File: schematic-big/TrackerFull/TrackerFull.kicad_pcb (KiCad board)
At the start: 2 copper layers, 43.2 x 38.1 mm, 58 parts, among them J1 Conn_01x05_Male, J3 Screw_Terminal_01x02, J4 78646-3001, J5 Screw_Terminal_01x02, Q1 IRLML0030, Q2 IRLML5203, Q3 IRLML5203, SW1 SW_Push, U1 LP2985-3.3, U2 LIS3DSH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

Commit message: last changes
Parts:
- moved GSM1 1.33 mm to (203.9, 96.0)
- moved H4 0.28 mm to (202.3, 71.5)
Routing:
- net GNDREF: track 195.4 -> 256.1 mm, vias 28 -> 32
- net /ACCEL_INT1: track 41.3 -> 98.0 mm, vias 2 -> 3
- net /VBAT: track 19.1 -> 60.5 mm, vias 0 -> 3
- net /SIM_RST: track 0.00 -> 24.3 mm
- net /VSIM: track 0.00 -> 17.6 mm
- net /AVR_RST: track 10.4 -> 25.1 mm, vias 0 -> 2
- net /ACCEL_INT2: track 25.9 -> 34.4 mm
- net /SIM_IO: track 15.5 -> 21.1 mm
- net /V_BAT: track 23.9 -> 19.3 mm
- net BAT_IN: track 77.6 -> 81.0 mm, vias 4 -> 5
- net Net-(D1-Pad45): track 3.20 -> 1.76 mm
- net +5V: track 47.0 -> 48.2 mm
- net /ACCEL_SCL: track 8.27 -> 7.08 mm
- net /AVR_MOSI_SDA: track 26.4 -> 27.1 mm
- net /SIM_CLK: track 16.0 -> 16.6 mm
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- added copper zone on B.Cu, net BAT_IN
- added copper zone on F.Cu, net GNDREF
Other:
- outline, holes or cut-outs redrawn
- net class Default: clearance 0.2 -> 0.127
- rule trace_clearance: 0.2 -> 0.127
- rule trace_min: 0.2 -> 0.127
- rule via_min_drill: 0.3 -> 0.2
- rule via_min_size: 0.4 -> 0.2

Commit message: last changes
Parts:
- C1: value 4.7u -> 4.7uF
- C10: footprint Capacitor_SMD:C_0201_0603Metric -> Capacitor_SMD:C_0402_1005Metric
- C11, C18: footprint Capacitor_Tantalum_SMD:CP_EIA-3216-18_Kemet-A -> Capacitor_SMD:C_0603_1608Metric
- C12: footprint Capacitor_SMD:C_1206_3216Metric_Pad1.42x1.75mm_HandSolder -> Capacitor_Tantalum_SMD:CP_EIA-7343-31_Kemet-D
- C17: footprint Capacitor_SMD:C_1206_3216Metric_Pad1.42x1.75mm_HandSolder -> Capacitor_SMD:C_0603_1608Metric; moved to B.Cu
- C6: value C -> 4.7uF
- R10: value 100kOm -> 100K; footprint Resistor_SMD:R_0603_1608Metric -> Resistor_SMD:R_0805_2012Metric_Pad1.15x1.40mm_HandSolder
- R13, R17, R4: footprint Resistor_SMD:R_0603_1608Metric -> Resistor_SMD:R_0805_2012Metric_Pad1.15x1.40mm_HandSolder
- R14, R16: value 10000 -> 10K; footprint Resistor_SMD:R_0603_1608Metric -> Resistor_SMD:R_0805_2012Metric_Pad1.15x1.40mm_HandSolder
- R15: value 43000 -> 43K
- moved C17 13.1 mm to (199.6, 68.0), turned to 180 degrees
- moved C10 5.09 mm to (182.5, 79.6)
- moved C12 1.84 mm to (186.0, 75.7)
- moved Q2 0.73 mm to (178.4, 80.8)
- moved R2 0.40 mm to (181.7, 81.0), turned to 0 degrees
- moved D2 0.26 mm to (185.4, 75.7)
- moved R13 0.25 mm to (174.6, 102.1)
- moved R17 0.20 mm to (192.8, 80.1)
- moved C14 0.14 mm to (184.8, 81.0)
- moved C8 0.06 mm to (187.4, 81.0)
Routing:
- net GNDREF: track 256.1 -> 241.7 mm
- net Net-(C17-Pad2): track 2.04 -> 14.9 mm, vias 0 -> 1
- net Net-(D1-Pad15): track 4.34 -> 5.27 mm
- net /ACCEL_INT1: track 98.0 -> 98.9 mm
- net /VBAT: track 60.5 -> 59.7 mm
- net Net-(Q1-Pad3): track 13.7 -> 13.0 mm
- net BAT_IN: track 81.0 -> 81.6 mm

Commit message: schematic updated
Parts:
- added C19: 1uF, Capacitor_SMD:C_0603_1608Metric, F.Cu at (168.0, 93.0)
- added R5: 10K, Resistor_SMD:R_0805_2012Metric_Pad1.15x1.40mm_HandSolder, B.Cu at (175.4, 93.2)
- added R6: 470, Resistor_SMD:R_0603_1608Metric, F.Cu at (177.1, 99.2)
- added U7: MIC5504-3.3YM5, Package_TO_SOT_SMD:SOT-23-5, F.Cu at (163.8, 94.8)
- C1: value 4.7uF -> 2.2uF
- C12: footprint Capacitor_Tantalum_SMD:CP_EIA-7343-31_Kemet-D -> Capacitor_Tantalum_SMD:CP_EIA-6032-28_Kemet-C
- C17, D3: moved to F.Cu
- C2: footprint Capacitor_SMD:C_0603_1608Metric -> Capacitor_SMD:C_0805_2012Metric
- Q1: value IRLML0030 -> DMG2305UXQ
- Q2, Q3: value IRLML5203 -> DMG2305UXQ
- R10: value 100K -> 10K
- R12, R8: value 250 -> 150
- R3: value 10K -> 470; footprint Resistor_SMD:R_0805_2012Metric_Pad1.15x1.40mm_HandSolder -> Resistor_SMD:R_0603_1608Metric
- SW1: value SW_Push -> PTS647SK38SMTR2LFS; footprint Button_Switch_SMD:SW_Push_1P1T_NO_6x6mm_H9.5mm -> imported:PTS647SK38SMTR2LFS
- U1: value LP2985-3.3 -> LP2980IM5-3.6
- moved Q1 17.9 mm to (174.5, 100.5)
- moved C17 13.1 mm to (187.1, 71.6), turned to 0 degrees
- moved C4 7.22 mm to (177.0, 89.6), turned to 270 degrees
- moved Q3 5.89 mm to (171.8, 78.5)
- moved R3 5.51 mm to (170.5, 83.8)
- moved SW1 0.81 mm to (181.6, 94.8)
- moved C12 0.65 mm to (186.3, 76.3)
- moved C18 0.52 mm to (193.7, 75.9)
- moved D3 0.42 mm to (166.3, 76.4)
- renumbered GSM1 to U6
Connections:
- net /3.3v renamed /3.6v
- C9 pad 1: /VBAT -> Net-(C9-Pad1)
- D1 pad 23: (no net) -> /GPS_POWER
- D1 pad 51: /ACCEL_INT1 -> (no net)
- Q1 pad 1: /PWR_CTRL -> Net-(Q1-Pad1)
- Q1 pad 2: GNDREF -> /VBAT
- Q1 pad 3: Net-(Q1-Pad3) -> Net-(C9-Pad1)
- Q2 pad 1: Net-(Q1-Pad3) -> /PWR_CTRL
- R13 pad 1: /VBAT -> Net-(C9-Pad1)
- R3 pad 1: BAT_IN -> /PWR_CTRL
- R3 pad 2: Net-(Q1-Pad3) -> Net-(R3-Pad2)
- SW1 pad 2: GNDREF -> /AVR_RST
- U3 pad 3: /PWR_CTRL -> Net-(R3-Pad2)
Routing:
- net /ACCEL_INT1: track 98.9 -> 13.2 mm, vias 3 -> 0
- net Net-(C17-Pad2): track 14.9 -> 1.71 mm, vias 1 -> 0
- net Net-(Q1-Pad3): track 13.0 -> 0.00 mm, vias 2 -> 0
- net GNDREF: track 241.7 -> 253.7 mm, vias 32 -> 34
- net +5V: track 48.2 -> 58.6 mm, vias 4 -> 3
- net /GPS_POWER: track 0.00 -> 7.03 mm
- net /V_BAT: track 19.3 -> 13.6 mm
- net BAT_IN: track 81.6 -> 76.6 mm
- net /ACCEL_CS: track 6.77 -> 10.7 mm, vias 0 -> 1
- net /ACCEL_INT2: track 34.4 -> 30.5 mm
- net /AVR_RST: track 25.1 -> 21.8 mm, vias 2 -> 0
- net Net-(R3-Pad2): track 0.00 -> 2.60 mm
- net /CHARGER_VDD: track 33.3 -> 35.7 mm, vias 8 -> 6
- net /PWR_CTRL: track 8.43 -> 10.8 mm
- net Net-(C9-Pad1): track 0.00 -> 2.19 mm, vias 0 -> 1
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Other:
- board size 43.2 x 38.1 mm -> 43.2 x 38 mm
- rule via_min_drill: 0.2 -> 0.3
- rule via_min_size: 0.2 -> 0.3

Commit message: next milestone
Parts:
- removed C13, C9: 4.7uF, Capacitor_SMD:C_0603_1608Metric
- removed Q1: DMG2305UXQ, Package_TO_SOT_SMD:SOT-23
- removed R13: 100K, Resistor_SMD:R_0805_2012Metric_Pad1.15x1.40mm_HandSolder
- removed R6: 470, Resistor_SMD:R_0603_1608Metric
- added ANT1: 1462350001, imported:ANT_1462350001, B.Cu at (167.3, 101.3)
- added L3: LQG15HS1N8B02, Inductor_SMD:L_0402_1005Metric, B.Cu at (178.7, 99.1)
- added U8: AP62301, Package_TO_SOT_SMD:SOT-563, F.Cu at (222.7, 79.2)
- C1: value 2.2uF -> 0.47uF
- H3, H4: moved to B.Cu
- L1: value LQG15HN27NJ -> LQG15HS5N1B02; footprint Inductor_SMD:L_01005_0402Metric -> Inductor_SMD:L_0402_1005Metric
- L2: value IHLP1212BZER2R2M11 -> MDWK4040T3R3MM; footprint Inductor_SMD:L_Vishay_IHLP-1212 -> Inductor_SMD:L_Taiyo-Yuden_MD-4040
- U1: value LP2980IM5-3.6 -> TLV62568DBV
- U5: value U.FL -> BGU7007,115; footprint mailboxNotifier:U.FL -> imported:PSON50P100X145X50-6N
- U7: value MIC5504-3.3YM5 -> MIC5232-2.5YD5
- moved U1 45.3 mm to (214.4, 82.8), turned to 0 degrees
- moved L1 8.83 mm to (170.6, 101.5)
- moved H3 7.08 mm to (175.6, 101.6)
- moved U7 6.58 mm to (170.4, 94.7), turned to 270 degrees
- moved U5 6.52 mm to (171.8, 99.8)
- moved D3 5.71 mm to (171.6, 78.6), turned to 180 degrees
- moved R11 5.35 mm to (170.5, 86.8), turned to 0 degrees
- moved Q3 5.30 mm to (177.1, 78.6)
- moved C19 2.53 mm to (170.3, 91.9), turned to 0 degrees
- moved Q2 1.90 mm to (178.4, 82.7)
- moved H4 1.62 mm to (202.6, 69.9)
- moved J1 1.21 mm to (203.6, 80.7)
- moved R1 1.16 mm to (172.2, 84.9)
- moved R3 0.73 mm to (170.6, 83.1)
- moved R15 0.56 mm to (197.4, 68.9)
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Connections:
- C1 pad 1: /3.6v -> /2.5v
- C2 pad 2: /3.6v -> /2.5v
- C3 pad 2: /3.6v -> /2.5v
- L1 pad 2: /GPS_RF -> Net-(L1-Pad2)
- U1 pad 1: BAT_IN -> (no net)
- U1 pad 2: GNDREF -> (no net)
- U1 pad 3: BAT_IN -> (no net)
- U1 pad 5: /3.6v -> (no net)
- U2 pad 1: /3.6v -> /2.5v
- U2 pad 14: /3.6v -> /2.5v
- U2 pad 15: /3.6v -> /2.5v
- U5 pad 3: /GPS_RF -> Net-(L1-Pad2)
- U7 pad 1: (no net) -> BAT_IN
- U7 pad 2: (no net) -> GNDREF
- U7 pad 3: (no net) -> BAT_IN
- U7 pad 5: (no net) -> /2.5v
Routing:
- net GNDREF: track 253.7 -> 207.8 mm, vias 34 -> 29
- net /VBAT: track 58.2 -> 38.7 mm
- net /2.5v: track 0.00 -> 13.1 mm
- net /3.6v: track 13.1 -> 0.00 mm
- net +5V: track 58.6 -> 47.1 mm, vias 3 -> 2
- net /LED_CTL: track 14.5 -> 7.71 mm
- net BAT_IN: track 76.6 -> 71.9 mm, vias 5 -> 4
- net /GPS_RF: track 6.27 -> 2.14 mm
- net Net-(ANT1-Pad1): track 7.57 -> 3.89 mm, vias 2 -> 0
- net /PWR_CTRL: track 10.8 -> 8.30 mm
- net /CHARGER_VDD: track 35.7 -> 38.0 mm
- net Net-(C9-Pad1): track 2.19 -> 0.00 mm, vias 1 -> 0
- net Net-(Q1-Pad1): track 1.83 -> 0.00 mm
- net /V_BAT: track 13.6 -> 11.8 mm
- net Net-(L1-Pad2): track 0.00 -> 1.43 mm
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- added copper zone on F.Cu, net BAT_IN
- removed copper zone on B.Cu, net BAT_IN
- removed copper zone on F.Cu, net GNDREF
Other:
- board size 43.2 x 38 mm -> 41.1 x 38 mm

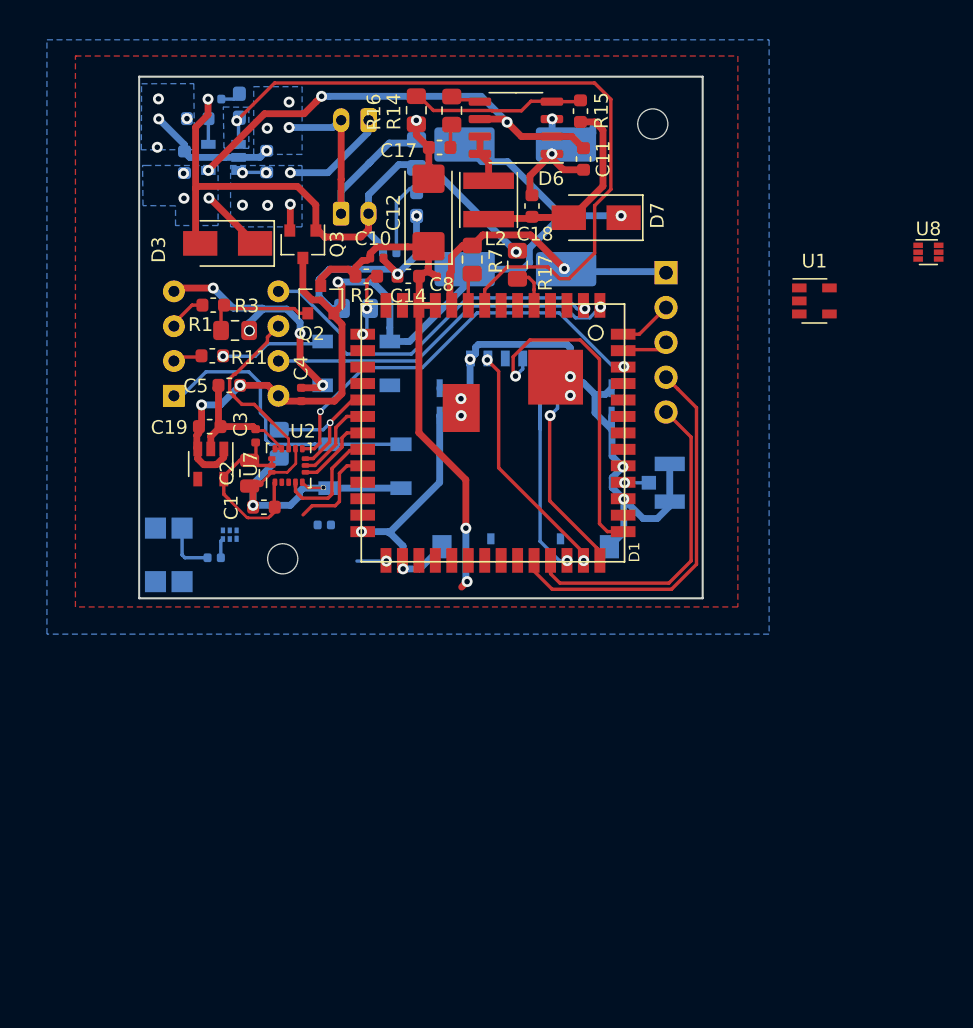
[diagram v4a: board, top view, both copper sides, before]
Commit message: GPS antenna on pcb
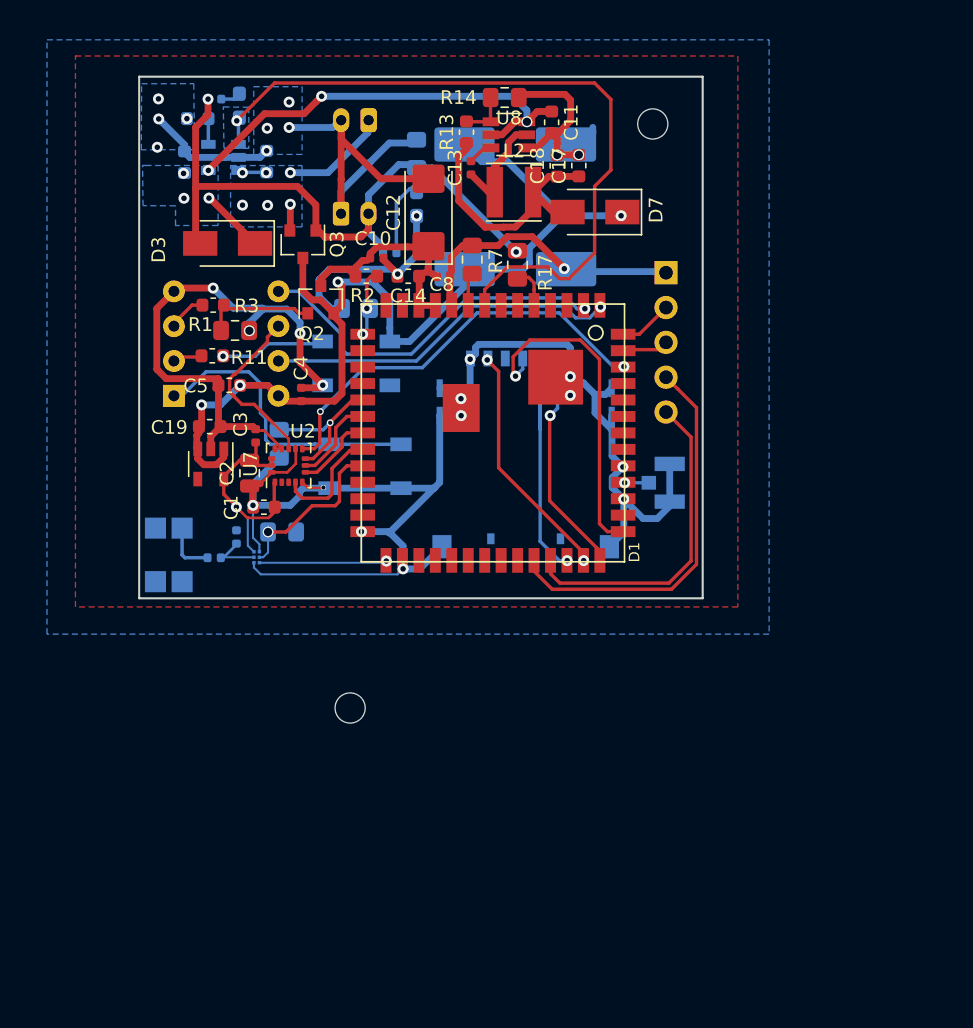
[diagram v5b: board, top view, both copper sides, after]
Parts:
- removed D6: APW7142, Package_SO:SOP-8_3.9x4.9mm_P1.27mm
- removed R15: 43K, Resistor_SMD:R_0603_1608Metric
- removed R16: 10K, Resistor_SMD:R_0805_2012Metric_Pad1.15x1.40mm_HandSolder
- removed U1: TLV62568DBV, Package_TO_SOT_SMD:SOT-23-5
- added C13: 100nF, Capacitor_SMD:C_0402_1005Metric, F.Cu at (189.4, 73.1)
- added R13: 43K, Resistor_SMD:R_0603_1608Metric, F.Cu at (189.0, 70.5)
- added R6: 10K, Resistor_SMD:R_0805_2012Metric_Pad1.15x1.40mm_HandSolder, B.Cu at (175.6, 99.6)
- C17: value 10uF -> 22uF
- J3: value Screw_Terminal_01x02 -> Battery
- J5: value Screw_Terminal_01x02 -> USB power
- U5: value BGU7007,115 -> BGU8019; footprint imported:PSON50P100X145X50-6N -> imported:SOT1232
- U8: footprint Package_TO_SOT_SMD:SOT-563 -> Package_TO_SOT_SMD:TSOT-23-6
- moved U8 31.8 mm to (192.1, 70.7), turned to 180 degrees
- moved H3 11.9 mm to (180.6, 112.5)
- moved C17 10.2 mm to (197.2, 72.9), turned to 90 degrees
- moved L3 6.46 mm to (172.3, 100.0), turned to 90 degrees
- moved R14 3.98 mm to (191.8, 67.9), turned to 0 degrees
- moved C11 3.54 mm to (195.2, 69.7)
- moved C18 3.46 mm to (195.6, 72.9)
- moved U5 2.56 mm to (173.7, 101.5), turned to 180 degrees
- moved L2 1.93 mm to (192.5, 74.8), turned to 0 degrees
- moved D7 0.42 mm to (198.4, 76.3)
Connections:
- C17 pad 1: GNDREF -> /APW_OUT
- C17 pad 2: Net-(C17-Pad2) -> GNDREF
- L1 pad 2: Net-(L1-Pad2) -> /GPS_SIGNAL
- L2 pad 1: /LX -> Net-(C13-Pad1)
- L3 pad 1: Net-(L1-Pad2) -> /GPS_SIGNAL
- R14 pad 1: Net-(D6-Pad5) -> Net-(R13-Pad2)
- R14 pad 2: Net-(C17-Pad2) -> GNDREF
- U5 pad 2: GNDREF -> /GPS_POWER
- U5 pad 3: Net-(L1-Pad2) -> /GPS_RF
- U5 pad 4: /VBAT -> GNDREF
- U5 pad 5: /GPS_POWER -> /GPS_SIGNAL
- U5 pad 6: /GPS_RF -> /2.5v
- U8 pad 1: (no net) -> GNDREF
- U8 pad 2: (no net) -> Net-(C13-Pad1)
- U8 pad 3: (no net) -> /CHARGER_VDD
- U8 pad 4: (no net) -> Net-(R13-Pad2)
- U8 pad 5: (no net) -> /CHARGER_VDD
- U8 pad 6: (no net) -> Net-(C13-Pad2)
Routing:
- net GNDREF: track 207.8 -> 244.6 mm, vias 29 -> 28
- net /VBAT: track 38.7 -> 16.6 mm, vias 2 -> 0
- net Net-(D6-Pad4): track 13.3 -> 0.00 mm
- net Net-(C13-Pad1): track 0.00 -> 7.88 mm
- net /GPS_RF: track 2.14 -> 9.31 mm
- net /GPS_POWER: track 7.03 -> 12.4 mm, vias 0 -> 1
- net /APW_OUT: track 15.4 -> 19.9 mm
- net /GPS_SIGNAL: track 0.00 -> 3.96 mm
- net /2.5v: track 13.1 -> 16.9 mm, vias 0 -> 1
- net Net-(R13-Pad2): track 0.00 -> 3.73 mm
- net /LX: track 3.54 -> 0.00 mm
- net Net-(D6-Pad5): track 2.11 -> 0.00 mm
- net Net-(C13-Pad2): track 0.00 -> 1.86 mm
- net Net-(C17-Pad2): track 1.71 -> 0.00 mm
- net Net-(L1-Pad2): track 1.43 -> 0.00 mm
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
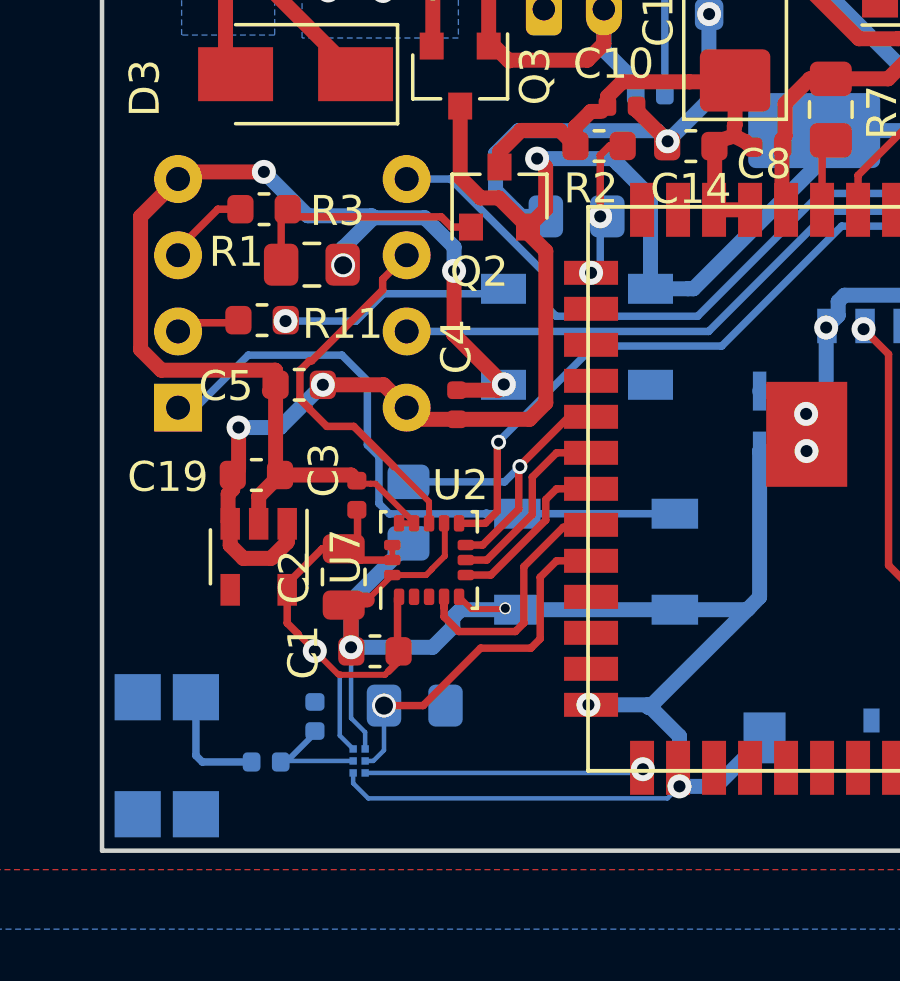
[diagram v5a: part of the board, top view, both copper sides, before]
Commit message: GPS antenna on pcb
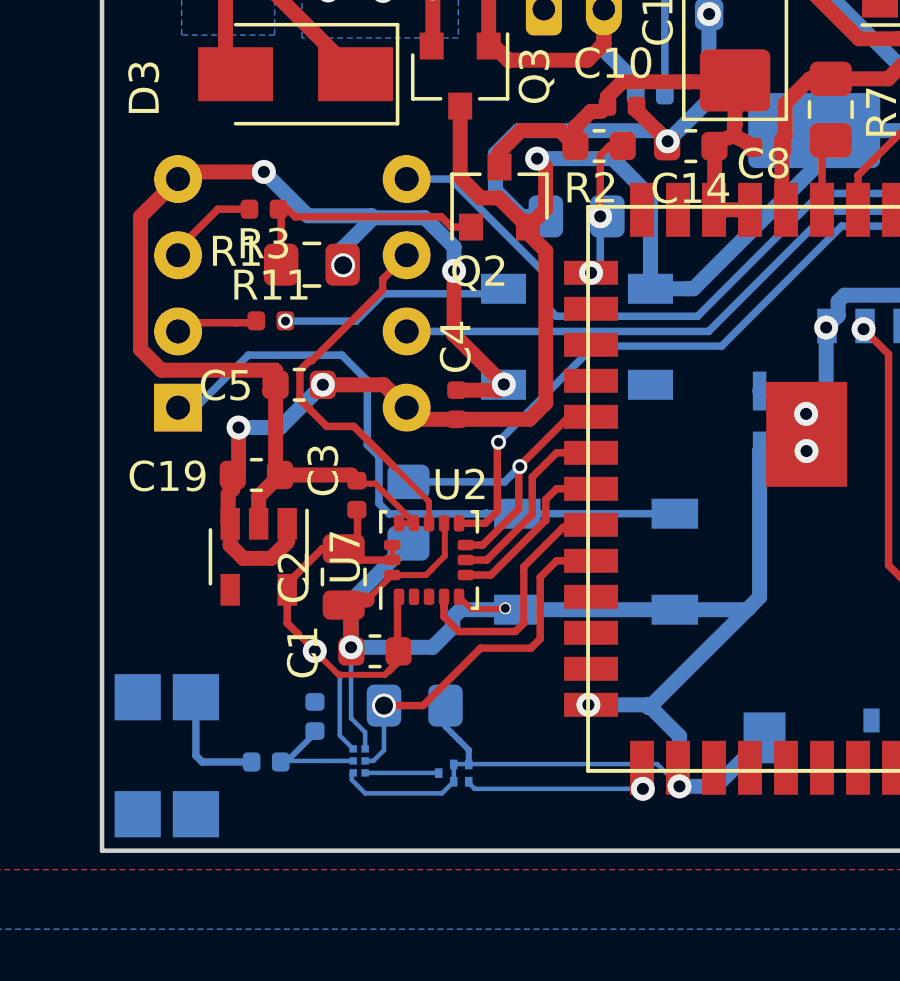
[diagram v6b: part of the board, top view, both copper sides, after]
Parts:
- added FL1: SF14-1582M5UUD2, Filter:Filter_1411-5_1.4x1.1mm, B.Cu at (176.9, 101.9)
- R11, R3: footprint Resistor_SMD:R_0603_1608Metric -> Resistor_SMD:R_0402_1005Metric
- moved R11 0.29 mm to (170.8, 86.8)
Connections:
- U5 pad 3: /GPS_RF -> Net-(FL1-Pad1)
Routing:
- net /GPS_RF: track 9.31 -> 5.89 mm
- net GNDREF: track 244.6 -> 247.7 mm
- net Net-(FL1-Pad1): track 0.00 -> 2.47 mm
- net Net-(R11-Pad1): track 2.17 -> 2.75 mm

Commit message: updated schematic
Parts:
- removed D7: D_Schottky, Diode_SMD:D_SMA
- removed R2: 200K, Resistor_SMD:R_0603_1608Metric
- removed R4: 100K, Resistor_SMD:R_0805_2012Metric_Pad1.15x1.40mm_HandSolder
- ANT1: value 1462350001 -> 146235-0001
- H3: moved to F.Cu
- U8: value AP62301 -> AP62301WU-7
- moved H3 46.3 mm to (216.6, 83.4)
- moved D3 0.57 mm to (171.1, 78.4)
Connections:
- C11 pad 1: /CHARGER_VDD -> /+5V
- C6 pad 2: /CHARGER_VDD -> /+5V
- D1 pad 15: Net-(D1-Pad15) -> /VBAT
- D3 pad 1: /CHARGER_VDD -> BAT_IN
- D3 pad 2: +5V -> /APW_OUT
- J5 pad 2: +5V -> /+5V
- Q3 pad 1: +5V -> /APW_OUT
- Q3 pad 2: /V_BAT -> BAT_IN
- Q3 pad 3: BAT_IN -> /V_BAT
- R10 pad 1: +5V -> /+5V
- R12 pad 1: +5V -> /+5V
- R17 pad 1: +5V -> /+5V
- R8 pad 1: +5V -> /+5V
- U4 pad 4: /CHARGER_VDD -> /+5V
- U8 pad 3: /CHARGER_VDD -> /+5V
- U8 pad 5: /CHARGER_VDD -> /+5V
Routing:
- net /+5V: track 0.00 -> 67.2 mm, vias 0 -> 13
- net +5V: track 47.1 -> 0.00 mm, vias 2 -> 0
- net /CHARGER_VDD: track 36.6 -> 0.00 mm, vias 6 -> 0
- net /APW_OUT: track 19.9 -> 39.1 mm
- net GNDREF: track 247.7 -> 234.8 mm, vias 28 -> 34
- net Net-(D1-Pad15): track 5.27 -> 0.00 mm, vias 2 -> 0
- net /VBAT: track 16.6 -> 21.4 mm
- net /V_BAT: track 11.8 -> 16.5 mm
- net BAT_IN: track 71.9 -> 72.5 mm, vias 4 -> 3
- added copper zone on B.Cu, net /+5V
- removed copper zone on B.Cu, net /CHARGER_VDD
